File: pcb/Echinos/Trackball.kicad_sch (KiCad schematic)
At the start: 8 parts, among them U6 PMW3360DM-T2QU, U7 VRH1902LTX

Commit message: ♻️ [PCB] - Add ferrite bead between shield and ground. Assign hand solder footprints whenever possible. Complete footprint assignation.
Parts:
- U7: footprint Package_TO_SOT_SMD:SOT-23-5 -> Package_TO_SOT_SMD:SOT-23-5_HandSoldering
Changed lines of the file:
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@@
       (effects (font (size 1.27 1.27)))
     )
-    (property "Footprint" "Package_TO_SOT_SMD:SOT-23-5" (at 151.13 38.735 0)
+    (property "Footprint" "Package_TO_SOT_SMD:SOT-23-5_HandSoldering" (at 151.13 38.735 0)
       (effects (font (size 1.27 1.27) italic) hide)
     )

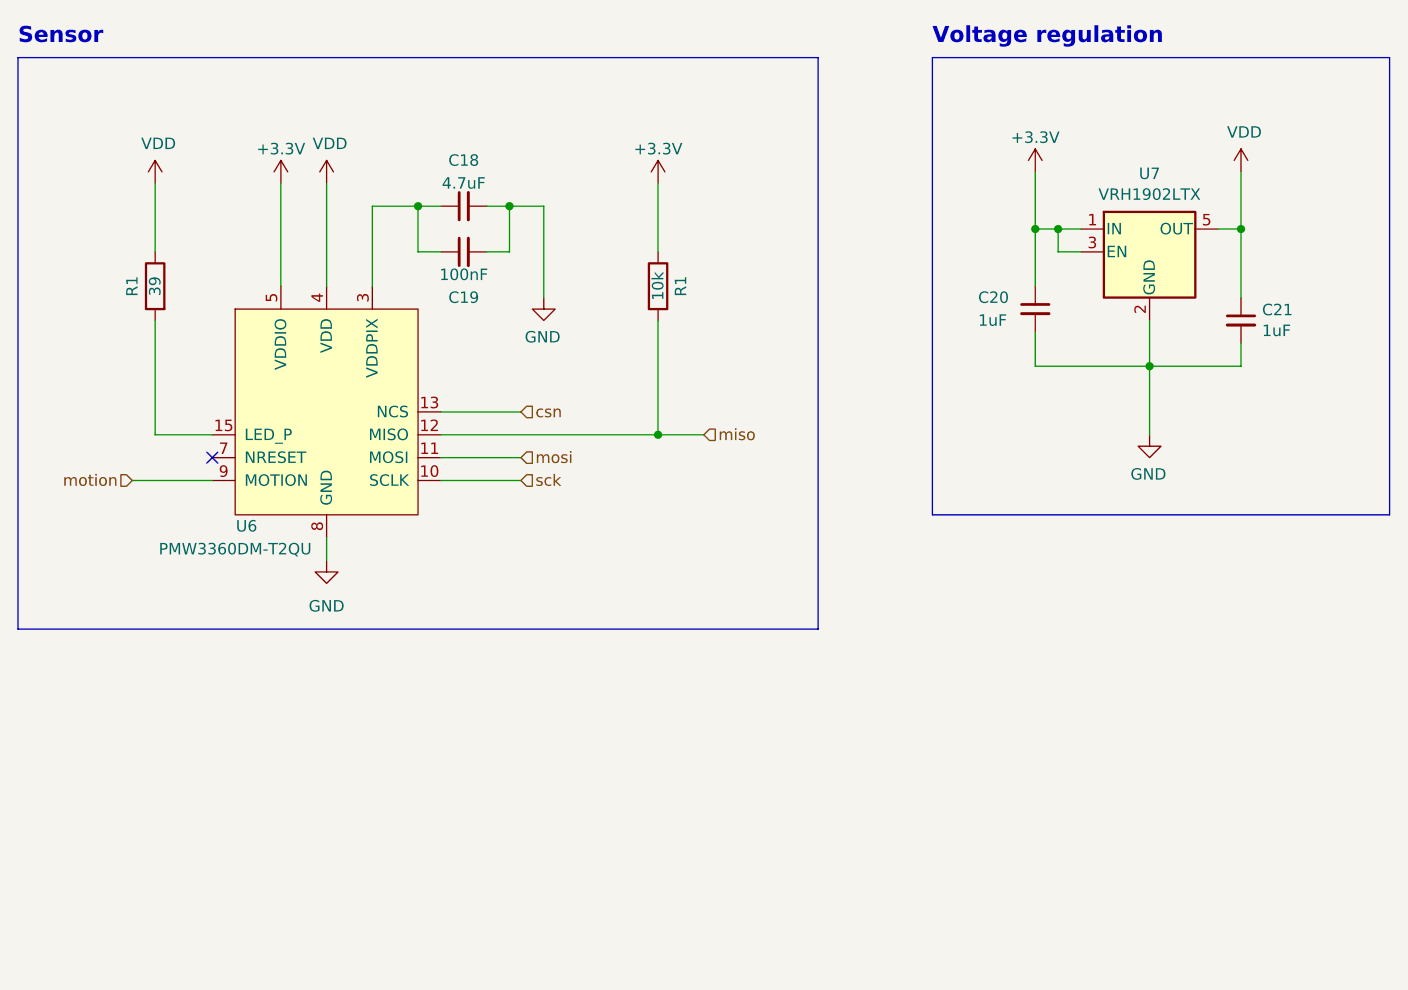
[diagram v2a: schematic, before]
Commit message: ✨ 🐛 ✅ [PCB] - Pass ERC test (exception to unconnected GPIO pins). Fix power symbol assignation to please Kicad. Fix duplicated line name (encoder / joystick) to please Kicad. Add trackball sensor connection documentation. Assign newly created footprints (encoder, joystick, switch).
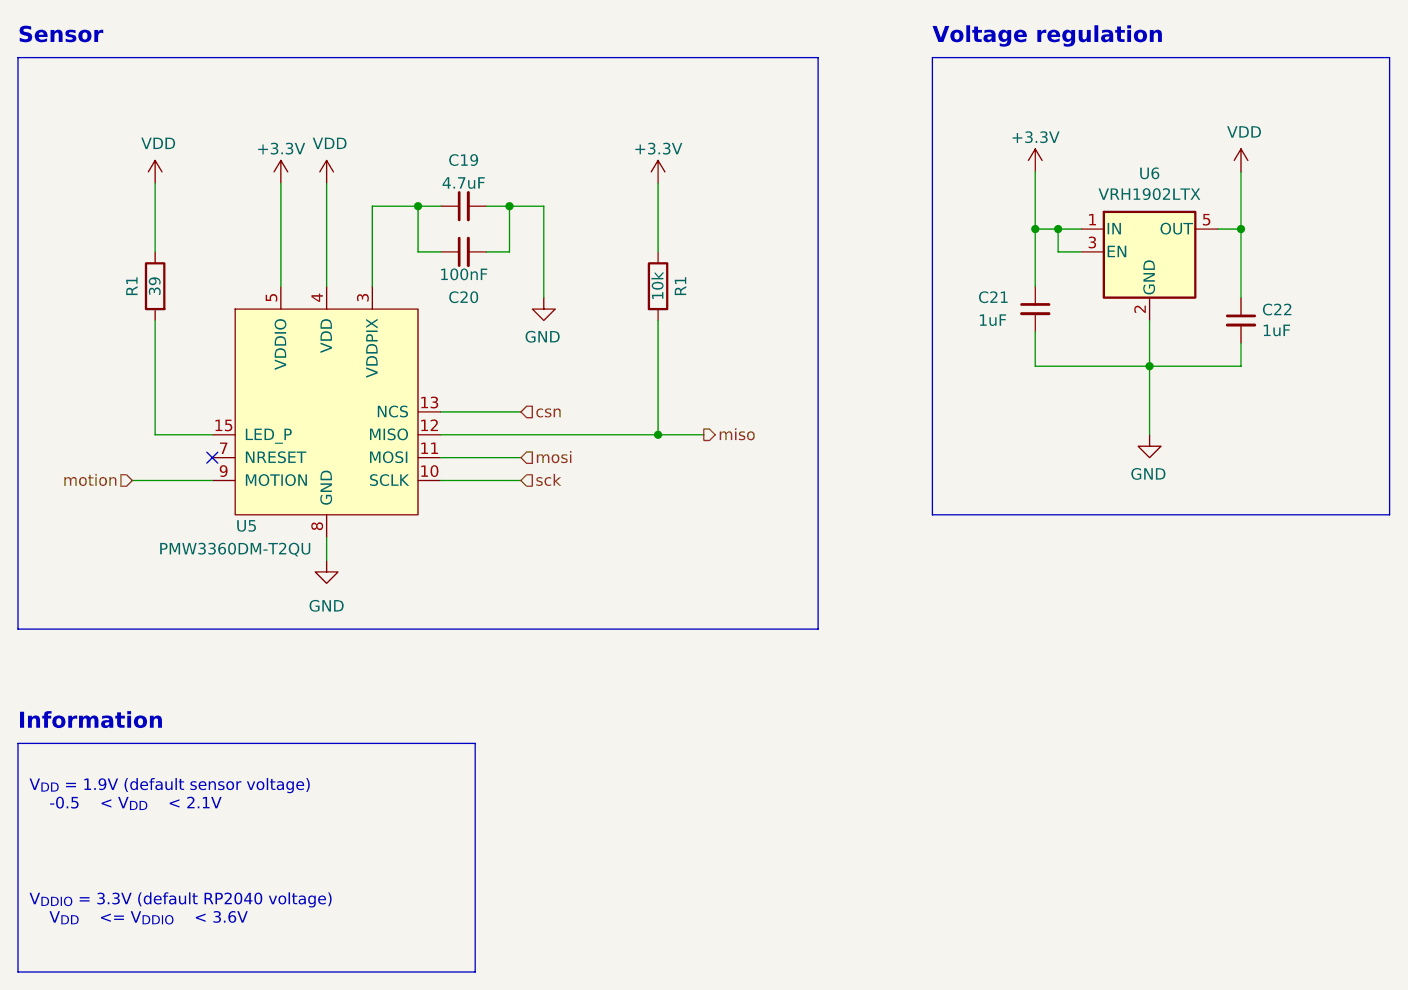
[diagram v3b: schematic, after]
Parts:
- renumbered C18 to C19, C19 to C20, C20 to C21, C21 to C22, U6 to U5, U7 to U6
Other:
- note added: "Information"
- note added: "V_{DDIO} = 3.3V (default RP2040 voltage) V_{DD} <= V_{DDIO} < 3.6V"
- note added: "V_{DD} = 1.9V (default sensor voltage) -0.5 < V_{DD} < 2.1V"

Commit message: ✨ [PCB] - Complete schema and PCB for left halve. All connections are made. Optional encoder on the top outer key Optional joystick on either outer thumb or above middle thumb. Optional power LED (jumpers) SATA to connect both sides VIK compatible (except for 5.0V track) with enough space on the inner side to clip a VIK module Remaining MCU pins exposed with a 2.54mm spaced header All VIK modules are not yet placed / routed.
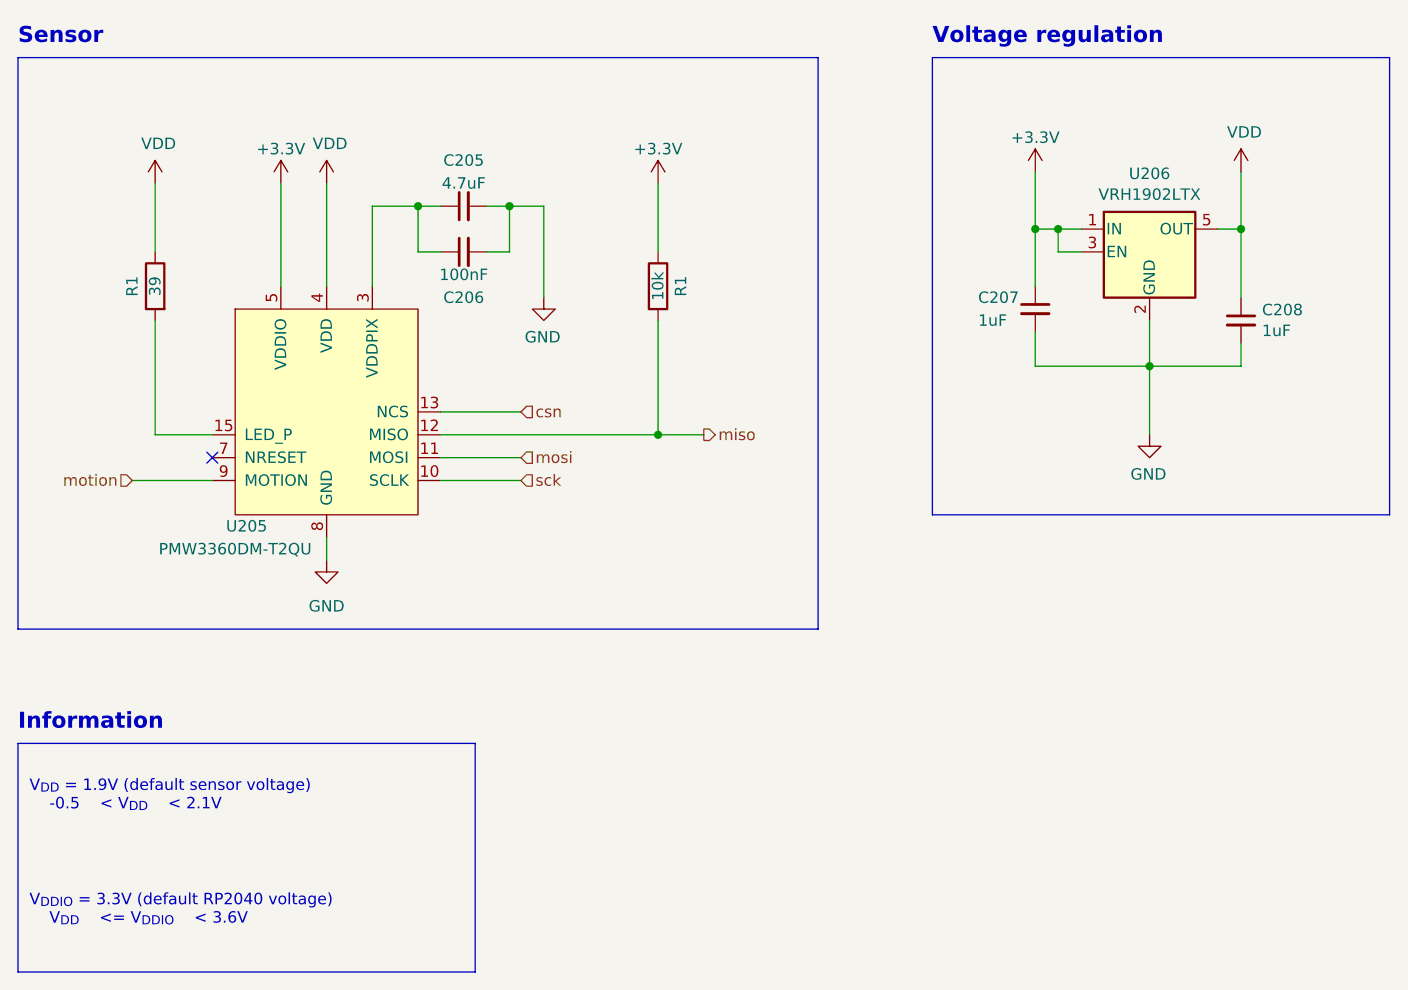
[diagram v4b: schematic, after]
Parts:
- renumbered C19 to C205, C20 to C206, C21 to C207, C22 to C208, U5 to U205, U6 to U206
